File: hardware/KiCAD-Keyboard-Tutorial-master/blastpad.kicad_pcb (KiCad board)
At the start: 2 copper layers, 191.7 x 108.5 mm, 58 parts, among them M3 MountingHole_3.2mm_M3, SW0:0 CTRL, SW0:1 SUPER, SW0:2 ALT, SW0:4 SPACE, SW1:1 SHIFT, SW1:2 Z, SW1:3 X, SW1:4 C, SW2:0 CAPS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

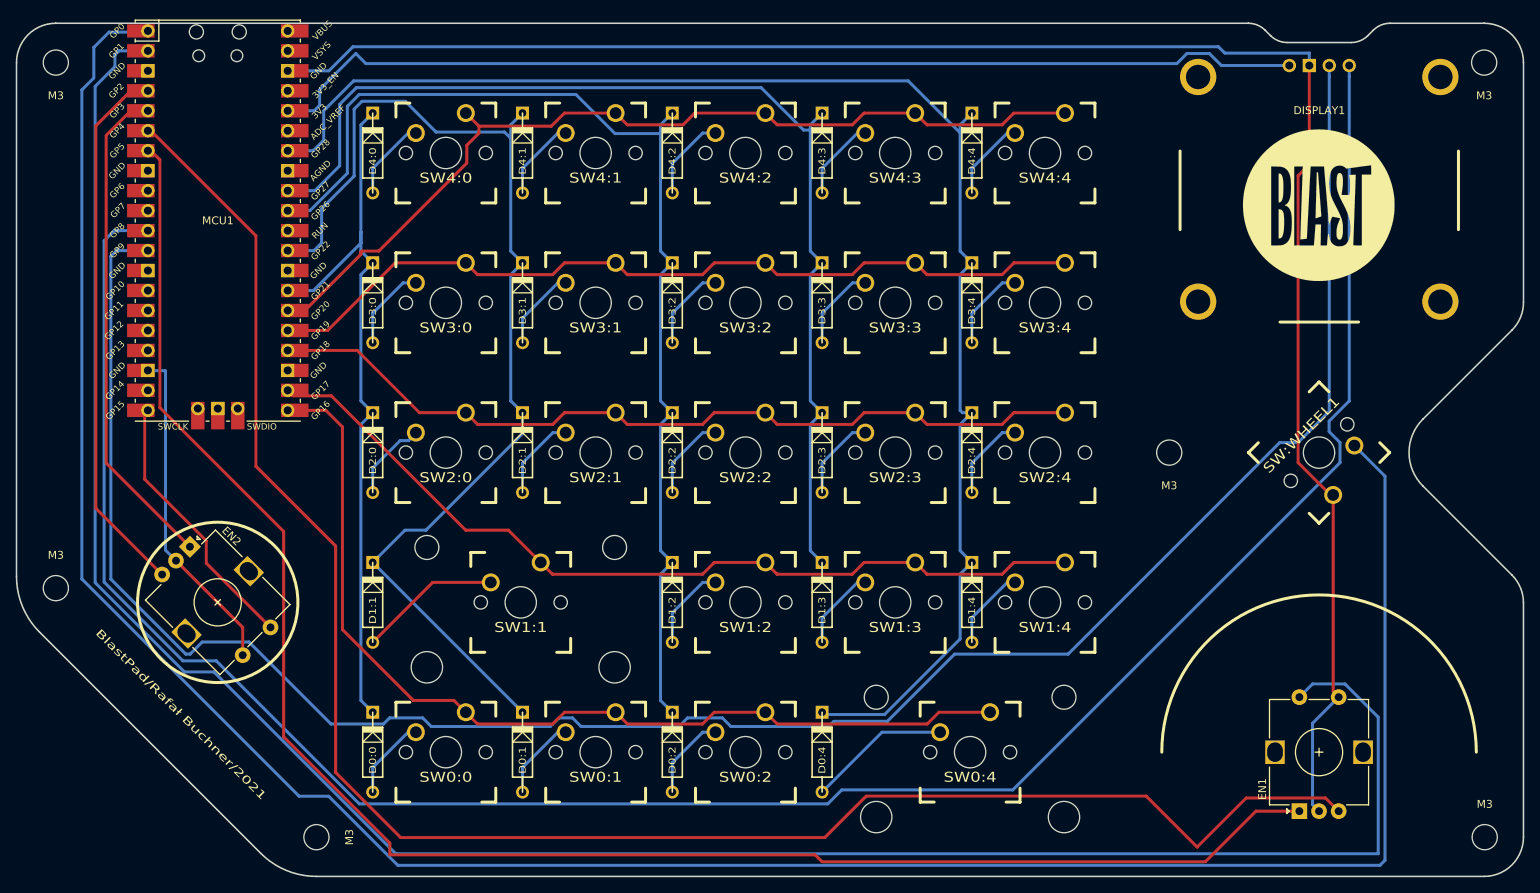
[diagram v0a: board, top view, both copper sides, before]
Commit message: update firmware to support CP 10.1.4
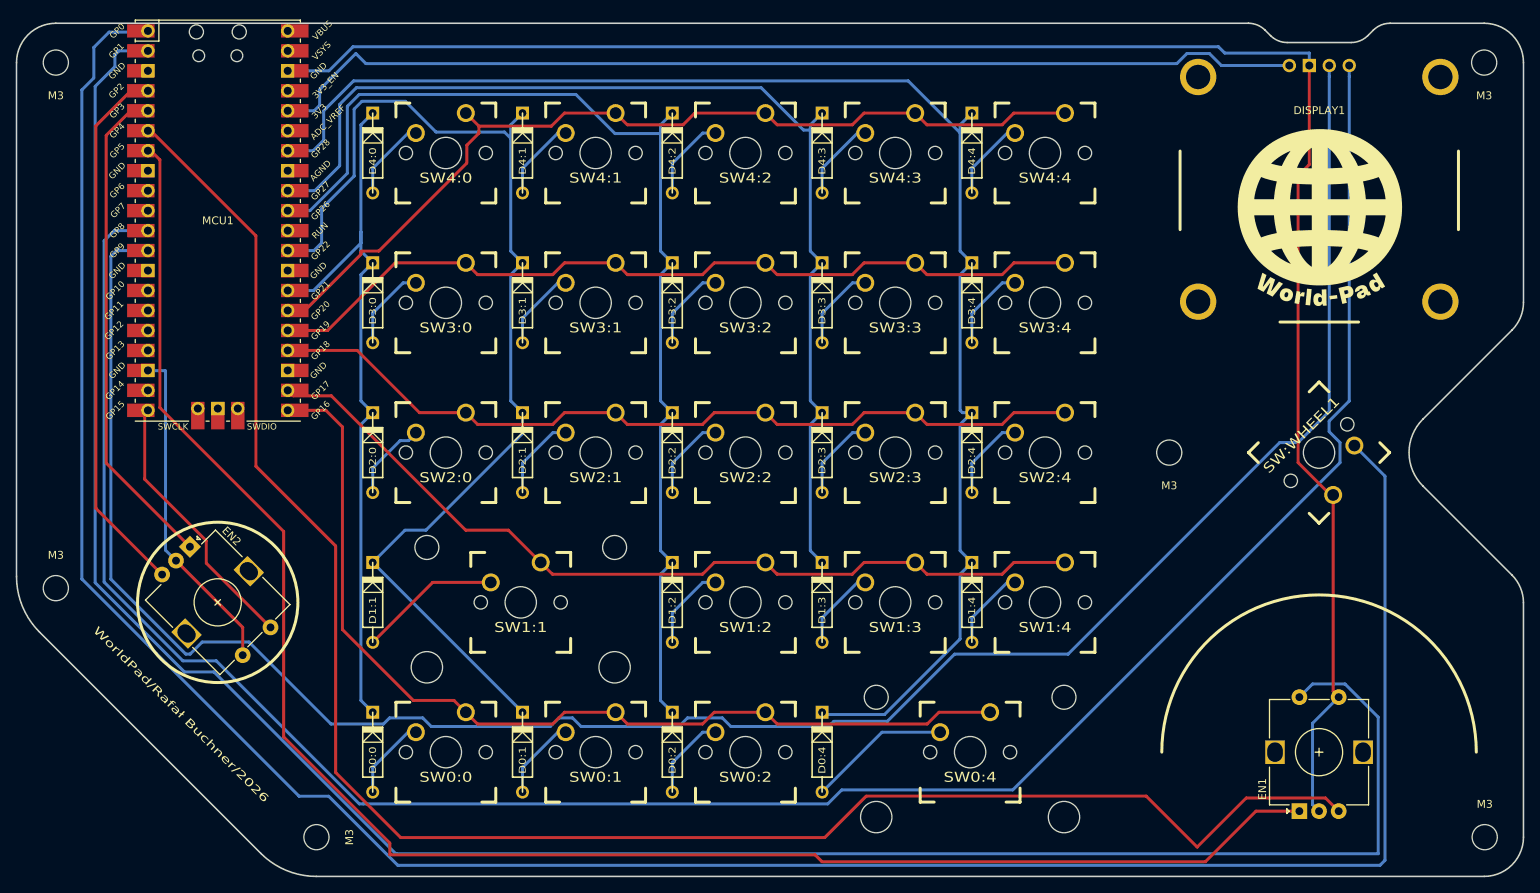
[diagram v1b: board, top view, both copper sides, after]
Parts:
- removed G***: LOGO, Blast_Logo:logo
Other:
- net class Default removed
- net class Thick removed
- board text added: "WorldPad/Rafał Buchner/2026"
- board text removed: "BlastPad/Rafał Buchner/2021"
